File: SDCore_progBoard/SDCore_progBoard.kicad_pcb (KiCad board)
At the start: 2 copper layers, 43 x 30.5 mm, 7 parts, among them U1 BL1117-33CX

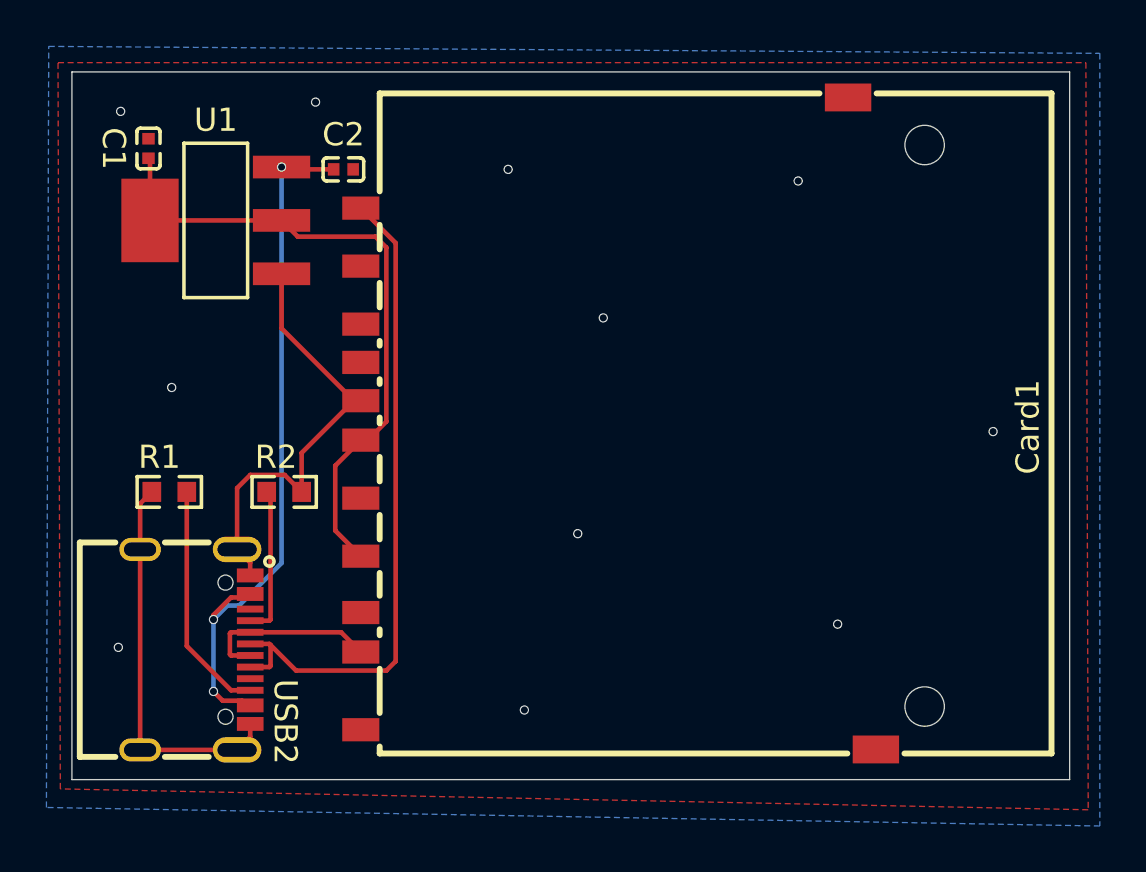
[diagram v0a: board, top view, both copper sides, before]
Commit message: Updated BOOTSEL logic
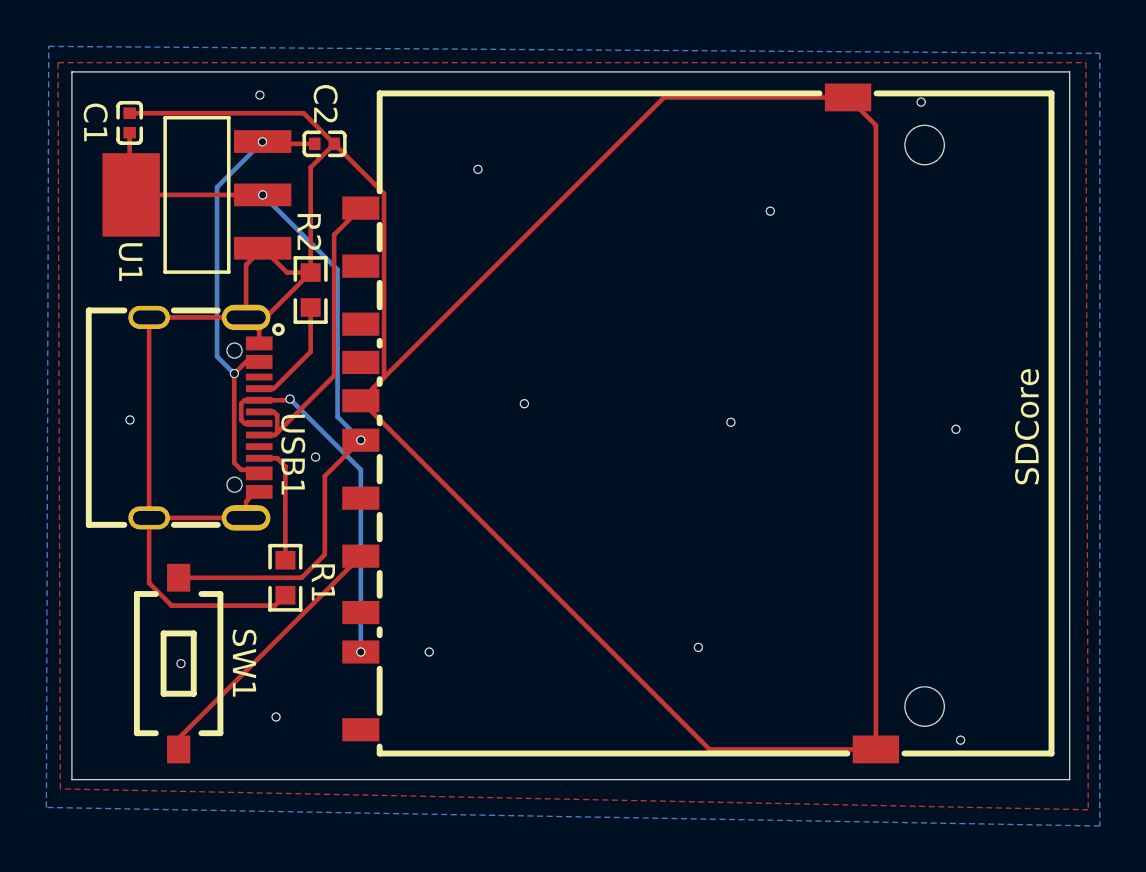
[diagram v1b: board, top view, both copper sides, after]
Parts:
- added SW1: TS-1101-C-W, JLCImport:TS-1101-C-W, F.Cu at (130.6, 118.0)
- moved USB1 10.0 mm to (131.7, 107.4)
- moved R2 8.77 mm to (136.3, 101.9), turned to -90 degrees
- moved R1 6.22 mm to (135.2, 114.3), turned to -90 degrees
- moved C2 1.37 mm to (136.9, 95.6)
- moved U1 1.37 mm to (131.4, 97.8)
- moved C1 1.37 mm to (128.5, 94.7)
- renumbered Card1 to SDCore, USB2 to USB1
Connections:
- SDCore pad 6: +3V3 -> Net-(Card1-VSS2)
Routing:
- net GND: track 36.7 -> 149.5 mm, vias 11 -> 14
- net Data_plus: track 28.9 -> 13.6 mm
- net Net-(Card1-VSS2): track 0.00 -> 11.6 mm
- net VBUS: track 30.4 -> 20.4 mm, vias 3 -> 2
- net Data_minus: track 7.81 -> 15.9 mm, vias 0 -> 2
- net Net-(USB1-CC2): track 10.2 -> 5.32 mm
- net +3V3: track 28.2 -> 33.0 mm, vias 0 -> 2
- net Net-(USB1-CC1): track 6.47 -> 4.78 mm

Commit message: More light changes
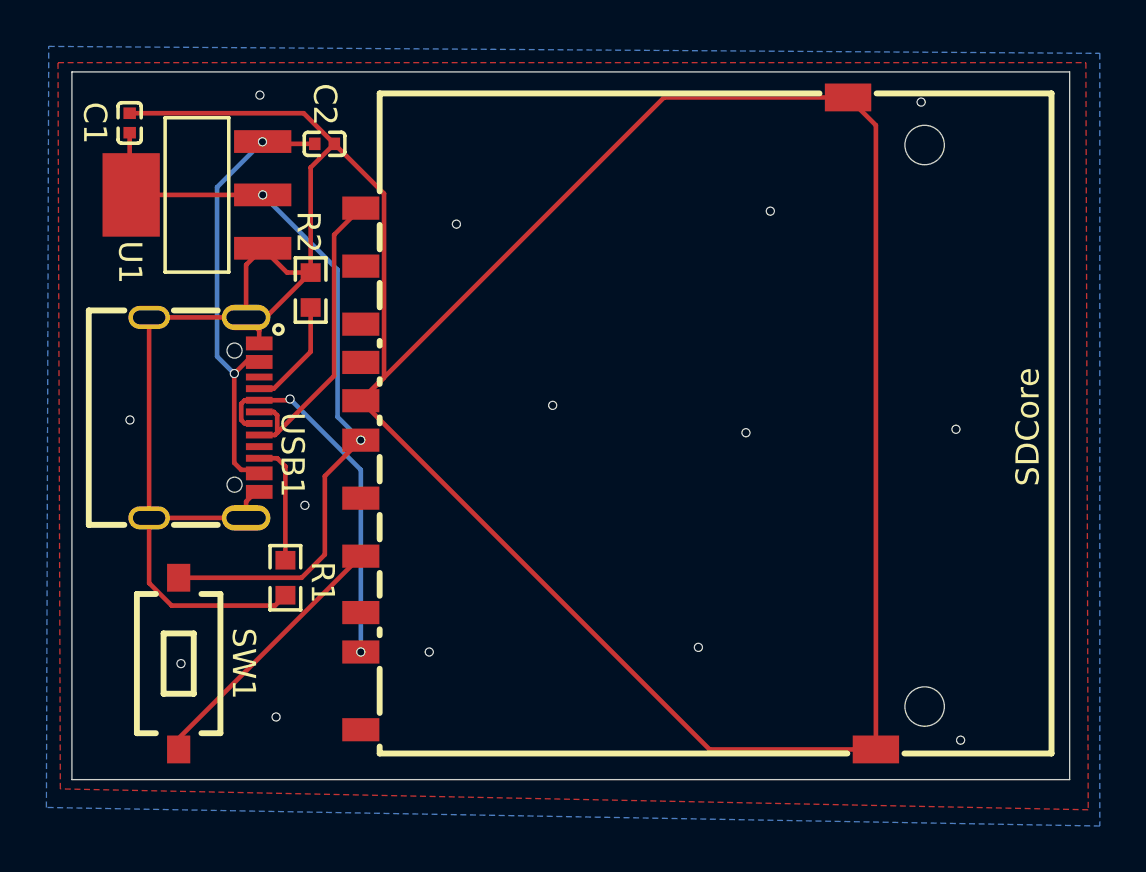
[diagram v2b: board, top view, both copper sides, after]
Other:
- board text added: "Github.com/Kniffler/SDCore"
- board text added: "I do pray this board works in the ways it is supposed to."
- board text added: "SDCore programmer board"
- board text added: "Version 0"

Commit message: Changed entirety of the progboard design to include a pin header, to make this devboard actually useful
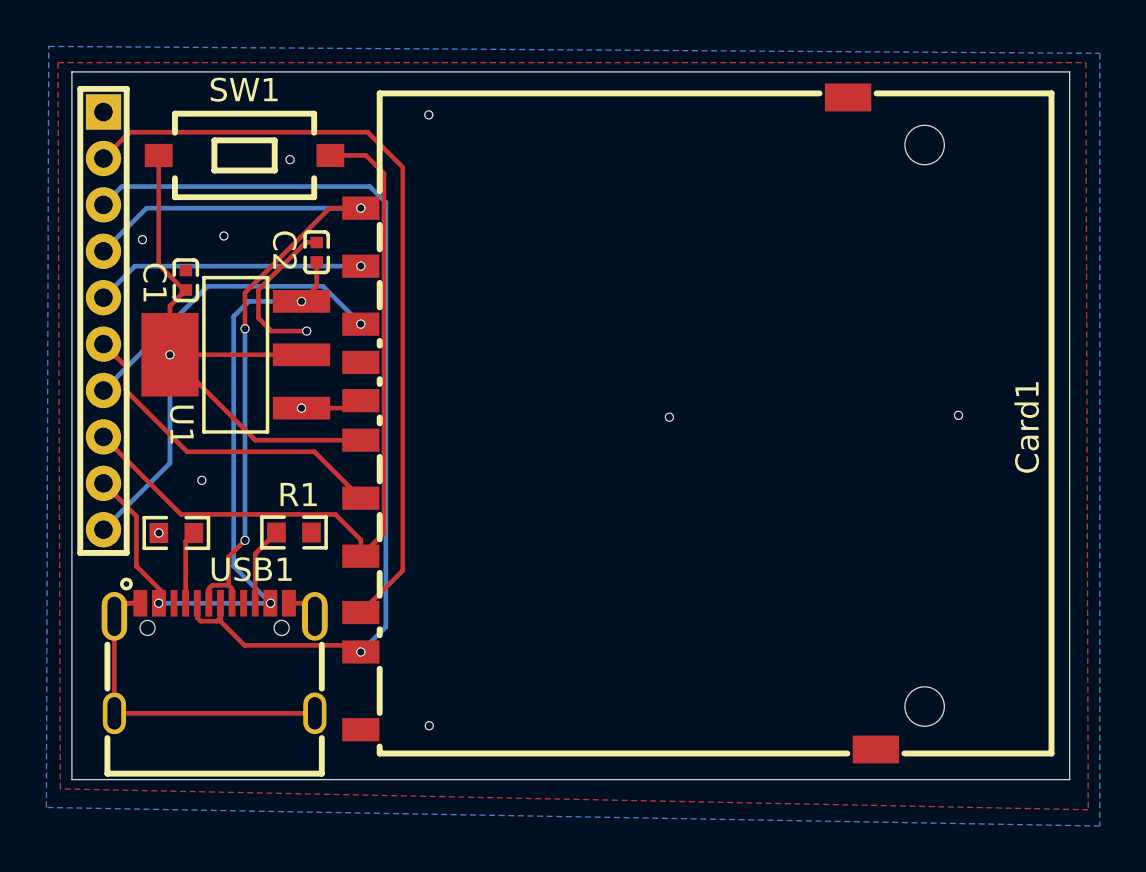
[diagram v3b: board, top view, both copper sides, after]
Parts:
- added H1: HX_PZ2_0-1X10P_ZZ, JLCImport:HX_PZ2_0-1X10P_ZZ, F.Cu at (127.4, 103.2)
- moved SW1 22.1 mm to (133.4, 96.1), turned to 0 degrees
- moved R2 12.0 mm to (130.5, 112.4), turned to 0 degrees
- moved USB1 10.4 mm to (132.2, 117.8), turned to 180 degrees
- moved C1 7.20 mm to (130.9, 101.5)
- moved U1 7.09 mm to (133.1, 104.7)
- moved C2 4.68 mm to (136.6, 100.3), turned to -90 degrees
- moved R1 1.98 mm to (135.6, 112.3), turned to 0 degrees
- renumbered SDCore to Card1
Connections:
- net Data_minus renamed DAT1 (USB-)
- net Data_plus renamed DAT2 (USB+)
- net Net-(Card1-VSS2) renamed PROG_PIN
- Card1 pad 1: unconnected-(Card1-CD/DAT3-Pad1) -> CD/DAT3 (CSn)
- Card1 pad 2: unconnected-(Card1-CMD-Pad2) -> CMD (TX MOSI)
- Card1 pad 5: unconnected-(Card1-CLK-Pad5) -> CLK (SCK)
- Card1 pad 7: unconnected-(Card1-DAT0-Pad7) -> DAT0 (RX MISO)
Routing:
- net GND: track 149.5 -> 26.0 mm, vias 14 -> 11
- net DAT0 (RX MISO): track 0.00 -> 33.9 mm
- net DAT1 (USB-): track 15.9 -> 42.6 mm, vias 2 -> 1
- net PROG_PIN: track 11.6 -> 33.2 mm
- net DAT2 (USB+): track 13.6 -> 33.6 mm, vias 0 -> 3
- net CLK (SCK): track 0.00 -> 15.1 mm
- net CMD (TX MOSI): track 0.00 -> 13.6 mm, vias 0 -> 1
- net CD/DAT3 (CSn): track 0.00 -> 11.7 mm, vias 0 -> 1
- net VBUS: track 20.4 -> 29.8 mm, vias 2 -> 3
- net Net-(USB1-CC2): track 5.32 -> 3.43 mm
- net Net-(USB1-CC1): track 4.78 -> 3.17 mm
- net +3V3: track 33.0 -> 33.6 mm, vias 2 -> 1
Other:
- board text added: "3V3"
- board text added: "CD/D3 CSn GPIO 9/5"
- board text added: "CLK SCK GPIO 10/6"
- board text added: "CMD TX/MOSI GPIO 11/7"
- board text added: "D0 RX/MISO GPIO 9/4"
- board text added: "D1 USB- GPIO 24/0"
- board text added: "D2 USB+ GPIO 25/1"
- board text added: "GND"
- board text added: "PROG pin"
- board text added: "VBUS"
